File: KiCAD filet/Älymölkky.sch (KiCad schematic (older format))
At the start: 44 parts, among them P0.18_TP1 Conn_01x01_Male, U1 nRF52810-QCxx, X1 32MHz Crystal, X2 32.768 kHz Crystal

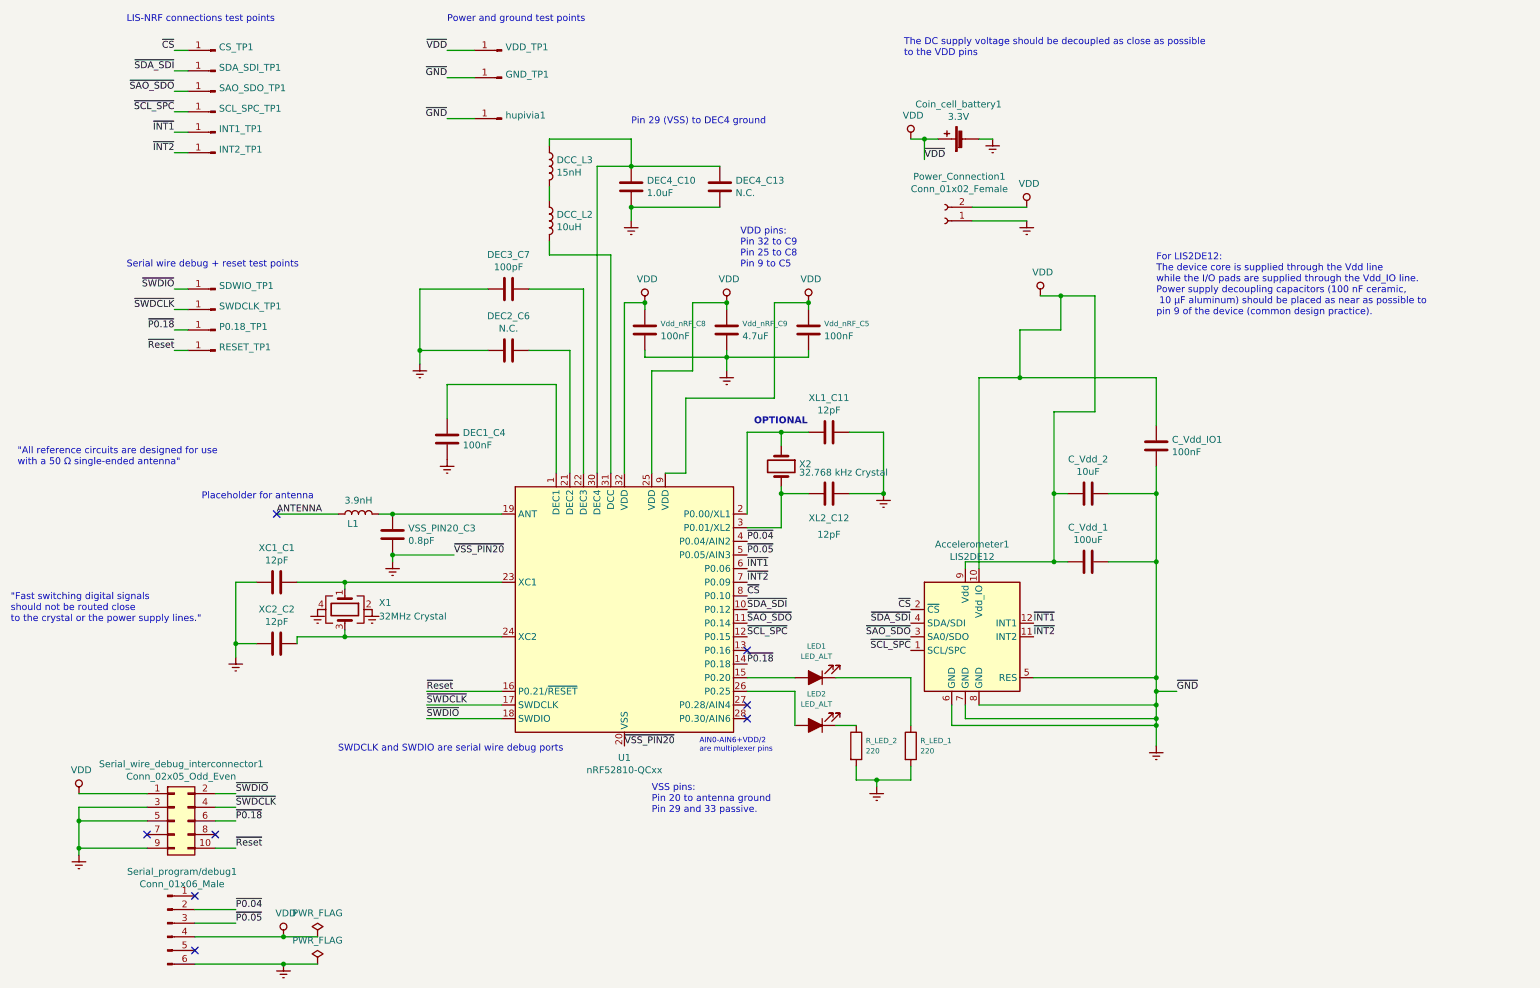
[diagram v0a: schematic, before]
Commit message: Added fuse, modified nRF and LIS footprints and started layout work
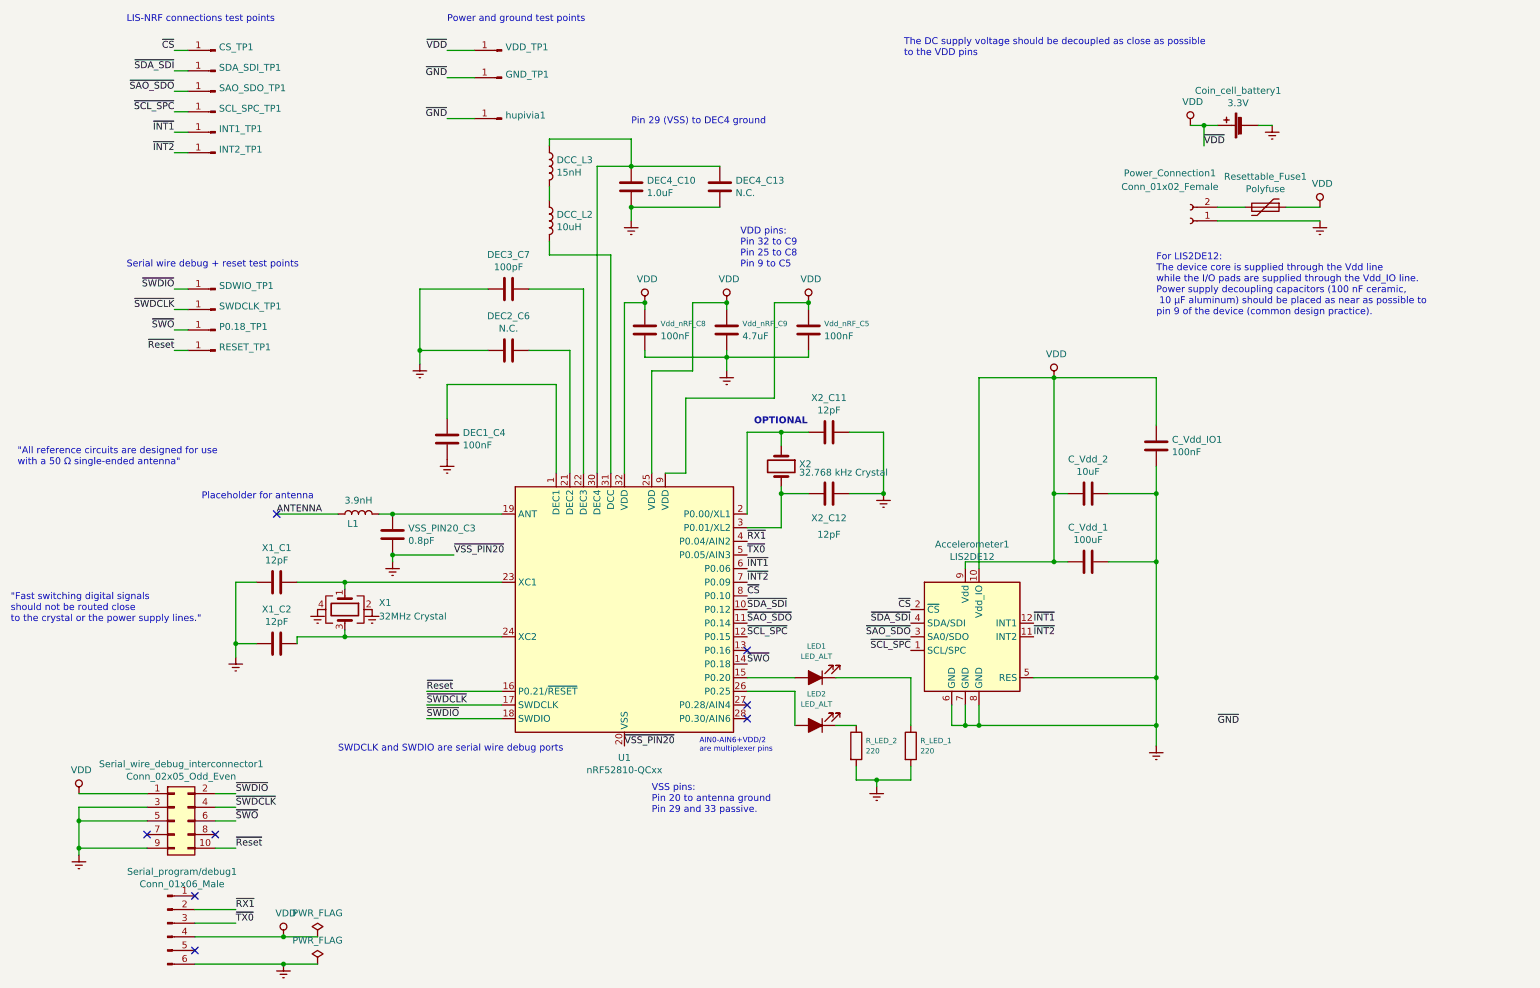
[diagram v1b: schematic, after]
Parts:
- added Resettable_Fuse1: Polyfuse, Resistor_SMD:R_0805_2012Metric_Pad1.15x1.40mm_HandSolder, symbol Device:Polyfuse
- renumbered XC1_C1 to X1_C1, XC2_C2 to X1_C2, XL1_C11 to X2_C11, XL2_C12 to X2_C12
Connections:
- net Earth: no longer GND_TP1.1 (Pin_1), hupivia1.1 (Pin_1)
- net VDD: now also Resettable_Fuse1.1; no longer Power_Connection1.2 (Pin_2)
- net ~P0.04 renamed ~RX1
- net ~P0.05 renamed ~TX0
- net ~P0.18 renamed ~SWO
- new net: Power_Connection1.2 (Pin_2), Resettable_Fuse1.2
- new net ~GND: GND_TP1.1 (Pin_1), hupivia1.1 (Pin_1)
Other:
- moved on the sheet: Coin_cell_battery1, Power_Connection1
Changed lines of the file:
@@
 Wire Wire Line
 	7650 4750 7650 3350
-Wire Wire Line
-	7650 3350 7950 3350
-Wire Wire Line
-	7950 3000 8250 3000
-Wire Wire Line
-	8250 3000 8250 2750
-Wire Wire Line
-	7950 3000 7950 3350
 $Comp
 L power:Earth #PWR0101
@@
 $EndComp
 Wire Wire Line
-	7650 5750 8950 5750
-Wire Wire Line
-	8950 5750 8950 5850
-Wire Wire Line
-	7550 5750 7550 5850
-Wire Wire Line
-	7550 5850 8950 5850
-Connection ~ 8950 5850
-Wire Wire Line
-	8950 5850 8950 5900
-Wire Wire Line
 	7450 5750 7450 5900
-Wire Wire Line
-	7450 5900 8950 5900
-Connection ~ 8950 5900
-Wire Wire Line
-	8950 5900 8950 6050
-Wire Wire Line
-	7950 3350 8950 3350
-Connection ~ 7950 3350
-Connection ~ 8950 5750
 $Comp
 L Device:C C_Vdd_2
@@
 Wire Wire Line
 	8950 4700 8950 5550
-Wire Wire Line
-	8200 4200 8200 3600
-Wire Wire Line
-	8500 3600 8500 2750
-Wire Wire Line
-	8500 2750 8250 2750
 Connection ~ 8200 4200
-Connection ~ 8250 2750
 $Comp
 L Device:C Vdd_nRF_C8
@@
 Text Label 2500 4350 0    50   ~ 0
 ANTENNA
-Wire Wire Line
-	8100 2750 8250 2750
-Wire Wire Line
-	8500 3600 8200 3600
 Text Label 7150 5150 2    50   ~ 0
 ~SDA_SDI
@@
 	8050 5550 8950 5550
 Connection ~ 8950 5550
-Wire Wire Line
-	8950 5550 8950 5650
 $Comp
 L Device:C Vdd_nRF_C9
@@
 L power:VDD #PWR0102
 U 1 1 5C5D4F0A
-P 8100 2750
-F 0 "#PWR0102" H 8100 2600 50  0001 C CNN
-F 1 "VDD" H 8117 2923 50  0000 C CNN
-F 2 "" H 8100 2750 50  0001 C CNN
-F 3 "" H 8100 2750 50  0001 C CNN
-	1    8100 2750
+P 8200 3350
+F 0 "#PWR0102" H 8200 3200 50  0001 C CNN
+F 1 "VDD" H 8217 3523 50  0000 C CNN
+F 2 "" H 8200 3350 50  0001 C CNN
+F 3 "" H 8200 3350 50  0001 C CNN
+	1    8200 3350
 	1    0    0    -1
 $EndComp
@@
 $EndComp
 $Comp
-L Device:C XC1_C1
+L Device:C X1_C1
 U 1 1 5C620184
 P 2500 4850
-F 0 "XC1_C1" V 2248 4850 50  0000 C CNN
+F 0 "X1_C1" V 2248 4850 50  0000 C CNN
 F 1 "12pF" V 2339 4850 50  0000 C CNN
 F 2 "Capacitor_SMD:C_0402_1005Metric" H 2538 4700 50  0001 C CNN
@@
 $EndComp
 $Comp
-L Device:C XC2_C2
+L Device:C X1_C2
 U 1 1 5C6201DB
 P 2500 5300
-F 0 "XC2_C2" V 2248 5300 50  0000 C CNN
+F 0 "X1_C2" V 2248 5300 50  0000 C CNN
 F 1 "12pF" V 2339 5300 50  0000 C CNN
 F 2 "Capacitor_SMD:C_0402_1005Metric" H 2538 5150 50  0001 C CNN
@@
 $EndComp
 $Comp
-L Device:C XL1_C11
+L Device:C X2_C11
 U 1 1 5C6386F1
 P 6550 3750
-F 0 "XL1_C11" V 6298 3750 50  0000 C CNN
+F 0 "X2_C11" V 6298 3750 50  0000 C CNN
 F 1 "12pF" V 6389 3750 50  0000 C CNN
 F 2 "Capacitor_SMD:C_0402_1005Metric" H 6588 3600 50  0001 C CNN
@@
 $EndComp
 $Comp
-L Device:C XL2_C12
+L Device:C X2_C12
 U 1 1 5C638747
 P 6550 4200
-F 0 "XL2_C12" V 6700 4200 50  0000 C TNN
+F 0 "X2_C12" V 6700 4200 50  0000 C TNN
 F 1 "12pF" V 6850 4200 50  0000 C CNN
 F 2 "Capacitor_SMD:C_0402_1005Metric" H 6588 4050 50  0001 C CNN
@@
 L Device:Battery_Cell Coin_cell_battery1
 U 1 1 5C63C076
-P 7550 1600
-F 0 "Coin_cell_battery1" V 7805 1650 50  0000 C CNN
-F 1 "3.3V" V 7714 1650 50  0000 C CNN
-F 2 "" V 7550 1660 50  0001 C CNN
-F 3 "~" V 7550 1660 50  0001 C CNN
-	1    7550 1600
+P 9600 1500
+F 0 "Coin_cell_battery1" V 9855 1550 50  0000 C CNN
+F 1 "3.3V" V 9764 1550 50  0000 C CNN
+F 2 "" V 9600 1560 50  0001 C CNN
+F 3 "~" V 9600 1560 50  0001 C CNN
+	1    9600 1500
 	0    -1   -1   0
 $EndComp
@@
 L power:Earth #PWR0113
 U 1 1 5C6419EB
-P 7750 1600
-F 0 "#PWR0113" H 7750 1350 50  0001 C CNN
-F 1 "Earth" H 7750 1450 50  0001 C CNN
-F 2 "" H 7750 1600 50  0001 C CNN
-F 3 "~" H 7750 1600 50  0001 C CNN
-	1    7750 1600
+P 9800 1500
+F 0 "#PWR0113" H 9800 1250 50  0001 C CNN
+F 1 "Earth" H 9800 1350 50  0001 C CNN
+F 2 "" H 9800 1500 50  0001 C CNN
+F 3 "~" H 9800 1500 50  0001 C CNN
+	1    9800 1500
 	1    0    0    -1
 $EndComp
@@
 L power:VDD #PWR0114
 U 1 1 5C641A7C
-P 7150 1600
-F 0 "#PWR0114" H 7150 1450 50  0001 C CNN
-F 1 "VDD" H 7167 1773 50  0000 C CNN
-F 2 "" H 7150 1600 50  0001 C CNN
-F 3 "" H 7150 1600 50  0001 C CNN
-	1    7150 1600
-	1    0    0    -1
-$EndComp
-Wire Wire Line
-	7750 1600 7650 1600
-Wire Wire Line
-	7150 1600 7250 1600
+P 9200 1500
+F 0 "#PWR0114" H 9200 1350 50  0001 C CNN
+F 1 "VDD" H 9217 1673 50  0000 C CNN
+F 2 "" H 9200 1500 50  0001 C CNN
+F 3 "" H 9200 1500 50  0001 C CNN
+	1    9200 1500
+	1    0    0    -1
+$EndComp
+Wire Wire Line
+	9800 1500 9700 1500
+Wire Wire Line
+	9200 1500 9300 1500
 Text Label 1750 950  2    50   ~ 0
 ~CS
@@
 Wire Wire Line
 	1850 1700 1750 1700
-Text Label 7250 1750 0    50   ~ 0
+Text Label 9300 1650 0    50   ~ 0
 ~VDD
 Wire Wire Line
-	7250 1600 7250 1750
-Connection ~ 7250 1600
-Wire Wire Line
-	7250 1600 7350 1600
+	9300 1500 9300 1650
+Connection ~ 9300 1500
+Wire Wire Line
+	9300 1500 9400 1500
 Text Label 3750 950  2    50   ~ 0
 ~VDD
@@
 	-1   0    0    1
 $EndComp
-Text Label 9100 5650 0    50   ~ 0
+Text Label 9400 5900 0    50   ~ 0
 ~GND
-Wire Wire Line
-	9100 5650 8950 5650
-Connection ~ 8950 5650
-Wire Wire Line
-	8950 5650 8950 5750
 Text Label 3750 1150 2    50   ~ 0
 ~GND
@@
 NoConn ~ 2050 6700
 Text Label 5950 5450 0    50   ~ 0
-~P0.18
+~SWO
 Text Label 2200 6600 0    50   ~ 0
-~P0.18
+~SWO
 Wire Wire Line
 	2200 6400 2050 6400
@@
 $EndComp
 Text Label 5950 4550 0    50   ~ 0
-~P0.04
+~RX1
 Text Label 5950 4650 0    50   ~ 0
-~P0.05
+~TX0
 NoConn ~ 1900 7150
 NoConn ~ 1900 7550
 Text Label 2200 7250 0    50   ~ 0
-~P0.04
+~RX1
 Text Label 2200 7350 0    50   ~ 0
-~P0.05
+~TX0
 $Comp
 L power:VDD #PWR0118
@@
 $EndComp
 Text Label 1750 3000 2    50   ~ 0
-~P0.18
+~SWO
 Text Label 1750 3150 2    50   ~ 0
 ~Reset
@@
 L Connector:Conn_01x02_Female Power_Connection1
 U 1 1 5C6A2D8F
-P 7400 2200
-F 0 "Power_Connection1" H 7294 1875 50  0000 C CNN
-F 1 "Conn_01x02_Female" H 7294 1966 50  0000 C CNN
-F 2 "Connector_PinHeader_2.54mm:PinHeader_1x02_P2.54mm_Vertical" H 7400 2200 50  0001 C CNN
-F 3 "~" H 7400 2200 50  0001 C CNN
-	1    7400 2200
+P 9200 2200
+F 0 "Power_Connection1" H 9350 1850 50  0000 C CNN
+F 1 "Conn_01x02_Female" H 9350 1950 50  0000 C CNN
+F 2 "Connector_PinHeader_2.54mm:PinHeader_1x02_P2.54mm_Vertical" H 9200 2200 50  0001 C CNN
+F 3 "~" H 9200 2200 50  0001 C CNN
+	1    9200 2200
 	-1   0    0    1
 $EndComp
@@
 L power:VDD #PWR0120
 U 1 1 5C6A36D5
-P 8000 2100
-F 0 "#PWR0120" H 8000 1950 50  0001 C CNN
-F 1 "VDD" H 8017 2273 50  0000 C CNN
-F 2 "" H 8000 2100 50  0001 C CNN
-F 3 "" H 8000 2100 50  0001 C CNN
-	1    8000 2100
+P 10150 2100
+F 0 "#PWR0120" H 10150 1950 50  0001 C CNN
+F 1 "VDD" H 10167 2273 50  0000 C CNN
+F 2 "" H 10150 2100 50  0001 C CNN
+F 3 "" H 10150 2100 50  0001 C CNN
+	1    10150 2100
 	1    0    0    -1
 $EndComp
@@
 L power:Earth #PWR0121
 U 1 1 5C6A3736
-P 8000 2200
-F 0 "#PWR0121" H 8000 1950 50  0001 C CNN
-F 1 "Earth" H 8000 2050 50  0001 C CNN
-F 2 "" H 8000 2200 50  0001 C CNN
-F 3 "~" H 8000 2200 50  0001 C CNN
-	1    8000 2200
-	1    0    0    -1
-$EndComp
-Wire Wire Line
-	8000 2100 7600 2100
-Wire Wire Line
-	7600 2200 8000 2200
+P 10150 2200
+F 0 "#PWR0121" H 10150 1950 50  0001 C CNN
+F 1 "Earth" H 10150 2050 50  0001 C CNN
+F 2 "" H 10150 2200 50  0001 C CNN
+F 3 "~" H 10150 2200 50  0001 C CNN
+	1    10150 2200
+	1    0    0    -1
+$EndComp
 $Comp
 L power:Earth #PWR0122
@@
 Wire Wire Line
 	3750 1450 3950 1450
+$Comp
+L Device:Polyfuse Resettable_Fuse1
+U 1 1 5C6C0B83
+P 9750 2100
+F 0 "Resettable_Fuse1" V 9525 2100 50  0000 C CNN
+F 1 "Polyfuse" V 9616 2100 50  0000 C CNN
+F 2 "Resistor_SMD:R_0805_2012Metric_Pad1.15x1.40mm_HandSolder" H 9800 1900 50  0001 L CNN
+F 3 "~" H 9750 2100 50  0001 C CNN
+	1    9750 2100
+	0    1    1    0
+$EndComp
+Wire Wire Line
+	9400 2100 9600 2100
+Wire Wire Line
+	9900 2100 10150 2100
+Wire Wire Line
+	9400 2200 10150 2200
+Wire Wire Line
+	7650 3350 8200 3350
+Connection ~ 8200 3350
+Wire Wire Line
+	8200 3350 8950 3350
+Wire Wire Line
+	8200 3350 8200 4200
+Wire Wire Line
+	8950 5550 8950 5900
+Wire Wire Line
+	7450 5900 7550 5900
+Connection ~ 8950 5900
+Wire Wire Line
+	8950 5900 8950 6050
+Wire Wire Line
+	7550 5750 7550 5900
+Connection ~ 7550 5900
+Wire Wire Line
+	7550 5900 7650 5900
+Wire Wire Line
+	7650 5750 7650 5900
+Connection ~ 7650 5900
+Wire Wire Line
+	7650 5900 8950 5900
 $EndSCHEMATC

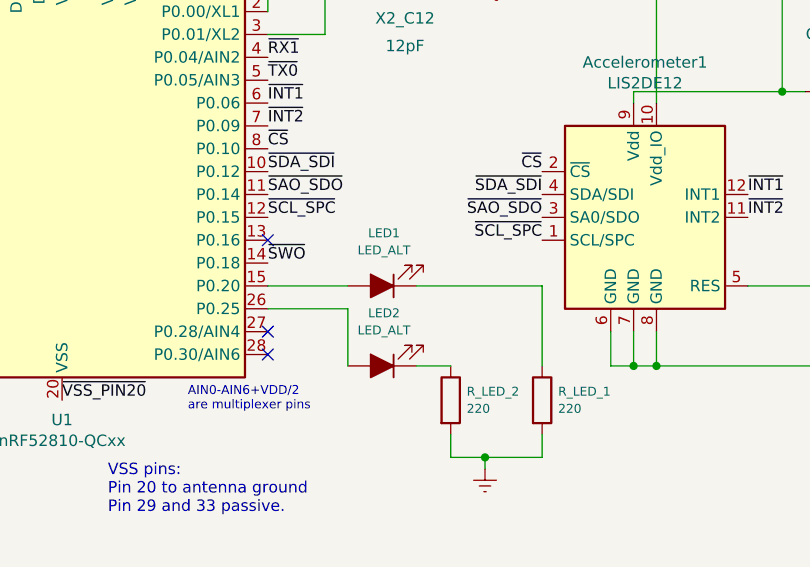
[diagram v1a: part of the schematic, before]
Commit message: Added more traces, shifted one pin's place and will shift more soon
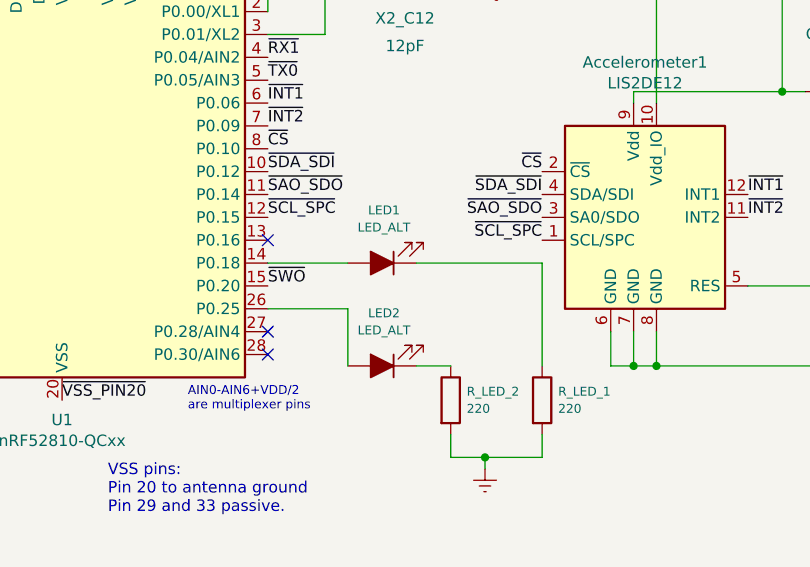
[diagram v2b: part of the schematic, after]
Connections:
- net ~SWO: now also U1.15 (P0.20); no longer U1.14 (P0.18)
- net at LED1.2 (A): now also U1.14 (P0.18); no longer U1.15 (P0.20)
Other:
- moved on the sheet: LED1
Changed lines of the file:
@@
 ~Reset
 NoConn ~ 2050 6700
-Text Label 5950 5450 0    50   ~ 0
+Text Label 5950 5550 0    50   ~ 0
 ~SWO
 Text Label 2200 6600 0    50   ~ 0
@@
 L Device:LED_ALT LED1
 U 1 1 5C6B701C
-P 6450 5550
-F 0 "LED1" H 6442 5319 39  0000 C CNN
-F 1 "LED_ALT" H 6442 5394 39  0000 C CNN
-F 2 "Resistor_SMD:R_0805_2012Metric_Pad1.15x1.40mm_HandSolder" H 6450 5550 50  0001 C CNN
-F 3 "~" H 6450 5550 50  0001 C CNN
-	1    6450 5550
+P 6450 5450
+F 0 "LED1" H 6442 5219 39  0000 C CNN
+F 1 "LED_ALT" H 6442 5294 39  0000 C CNN
+F 2 "Resistor_SMD:R_0805_2012Metric_Pad1.15x1.40mm_HandSolder" H 6450 5450 50  0001 C CNN
+F 3 "~" H 6450 5450 50  0001 C CNN
+	1    6450 5450
 	-1   0    0    1
 $EndComp
@@
 	-1   0    0    1
 $EndComp
-Wire Wire Line
-	5950 5550 6300 5550
 Wire Wire Line
 	5950 5650 6300 5650
@@
 Connection ~ 6900 6300
 Wire Wire Line
-	6600 5550 7150 5550
-Wire Wire Line
-	7150 5550 7150 5900
-Wire Wire Line
 	7150 6200 7150 6300
 Wire Wire Line
@@
 Wire Wire Line
 	7650 5900 8950 5900
+Wire Wire Line
+	5950 5450 6300 5450
+Wire Wire Line
+	7150 5450 6600 5450
+Wire Wire Line
+	7150 5450 7150 5900
 $EndSCHEMATC

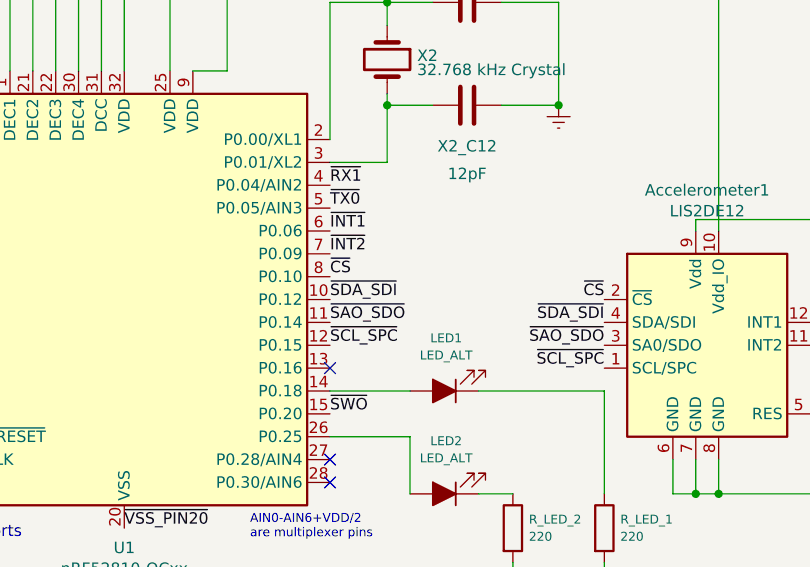
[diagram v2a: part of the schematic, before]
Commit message: Reorganized more pins, drew LIS traces
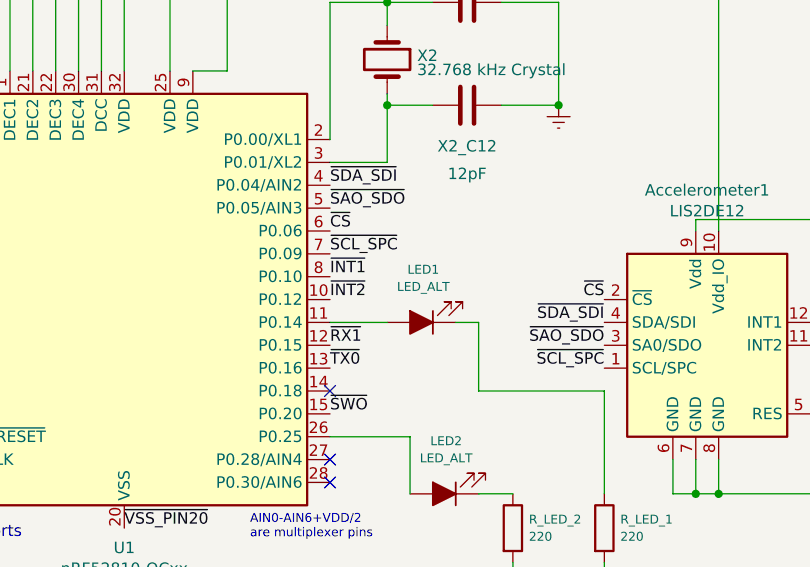
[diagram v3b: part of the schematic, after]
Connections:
- net ~CS: now also U1.6 (P0.06); no longer U1.8 (P0.10)
- net ~INT1: now also U1.8 (P0.10); no longer U1.6 (P0.06)
- net ~INT2: now also U1.10 (P0.12); no longer U1.7 (P0.09)
- net ~RX1: now also U1.12 (P0.15); no longer U1.4 (P0.04/AIN2)
- net ~SAO_SDO: now also U1.5 (P0.05/AIN3); no longer U1.11 (P0.14)
- net ~SCL_SPC: now also U1.7 (P0.09); no longer U1.12 (P0.15)
- net ~SDA_SDI: now also U1.4 (P0.04/AIN2); no longer U1.10 (P0.12)
- net ~TX0: now also U1.13 (P0.16); no longer U1.5 (P0.05/AIN3)
- net at LED1.2 (A): now also U1.11 (P0.14); no longer U1.14 (P0.18)
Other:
- moved on the sheet: LED1
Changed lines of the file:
@@
 Text Label 7150 5050 2    50   ~ 0
 ~CS
-Text Label 5950 4950 0    50   ~ 0
+Text Label 5950 4750 0    50   ~ 0
 ~CS
 $Comp
@@
 Text Label 7150 5150 2    50   ~ 0
 ~SDA_SDI
-Text Label 5950 5050 0    50   ~ 0
+Text Label 5950 4550 0    50   ~ 0
 ~SDA_SDI
 Text Label 7150 5250 2    50   ~ 0
 ~SAO_SDO
-Text Label 5950 5150 0    50   ~ 0
+Text Label 5950 4650 0    50   ~ 0
 ~SAO_SDO
 Text Label 7150 5350 2    50   ~ 0
 ~SCL_SPC
-Text Label 5950 5250 0    50   ~ 0
+Text Label 5950 4850 0    50   ~ 0
 ~SCL_SPC
 Text Label 8050 5150 0    50   ~ 0
 ~INT1
-Text Label 5950 4750 0    50   ~ 0
+Text Label 5950 4950 0    50   ~ 0
 ~INT1
 Text Label 8050 5250 0    50   ~ 0
 ~INT2
-Text Label 5950 4850 0    50   ~ 0
+Text Label 5950 5050 0    50   ~ 0
 ~INT2
 Wire Wire Line
@@
 Wire Wire Line
 	4150 5850 3600 5850
-NoConn ~ 5950 5350
 Text Notes 5600 6100 0    39   ~ 0
 AIN0-AIN6+VDD/2\nare multiplexer pins
@@
 L Device:LED_ALT LED1
 U 1 1 5C6B701C
-P 6450 5450
-F 0 "LED1" H 6442 5219 39  0000 C CNN
-F 1 "LED_ALT" H 6442 5294 39  0000 C CNN
-F 2 "Resistor_SMD:R_0805_2012Metric_Pad1.15x1.40mm_HandSolder" H 6450 5450 50  0001 C CNN
-F 3 "~" H 6450 5450 50  0001 C CNN
-	1    6450 5450
+P 6350 5150
+F 0 "LED1" H 6342 4919 39  0000 C CNN
+F 1 "LED_ALT" H 6342 4994 39  0000 C CNN
+F 2 "Resistor_SMD:R_0805_2012Metric_Pad1.15x1.40mm_HandSolder" H 6350 5150 50  0001 C CNN
+F 3 "~" H 6350 5150 50  0001 C CNN
+	1    6350 5150
 	-1   0    0    1
 $EndComp
@@
 	1    0    0    -1
 $EndComp
-Text Label 5950 4550 0    50   ~ 0
+Text Label 5950 5250 0    50   ~ 0
 ~RX1
-Text Label 5950 4650 0    50   ~ 0
+Text Label 5950 5350 0    50   ~ 0
 ~TX0
 NoConn ~ 1900 7150
@@
 	7650 5900 8950 5900
 Wire Wire Line
-	5950 5450 6300 5450
-Wire Wire Line
 	7150 5450 6600 5450
 Wire Wire Line
 	7150 5450 7150 5900
+Wire Wire Line
+	5950 5150 6200 5150
+Wire Wire Line
+	6500 5150 6600 5150
+Wire Wire Line
+	6600 5150 6600 5450
+NoConn ~ 5950 5450
 $EndSCHEMATC
